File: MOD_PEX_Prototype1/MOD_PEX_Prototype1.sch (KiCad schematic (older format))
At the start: 69 parts, among them CN1 CONN_PANNEL_2X2, CN2 CONN_PANNEL_2X2, J1 RJ45_CHAIN, J2 RJ45_CHAIN, P1 HEADER_3X1, P2 HEADER_5X2, P3 HEADER_5X2, P4 HEADER_2X1, Q1 MMBT3904, Q2 MMBT3904, SW1 SWITCH_HH, U1 LPC111X_LQFP48, U2 AP1117E50G, U3 AP1117E33G, U4 SN75176BDR, X1 10MHz

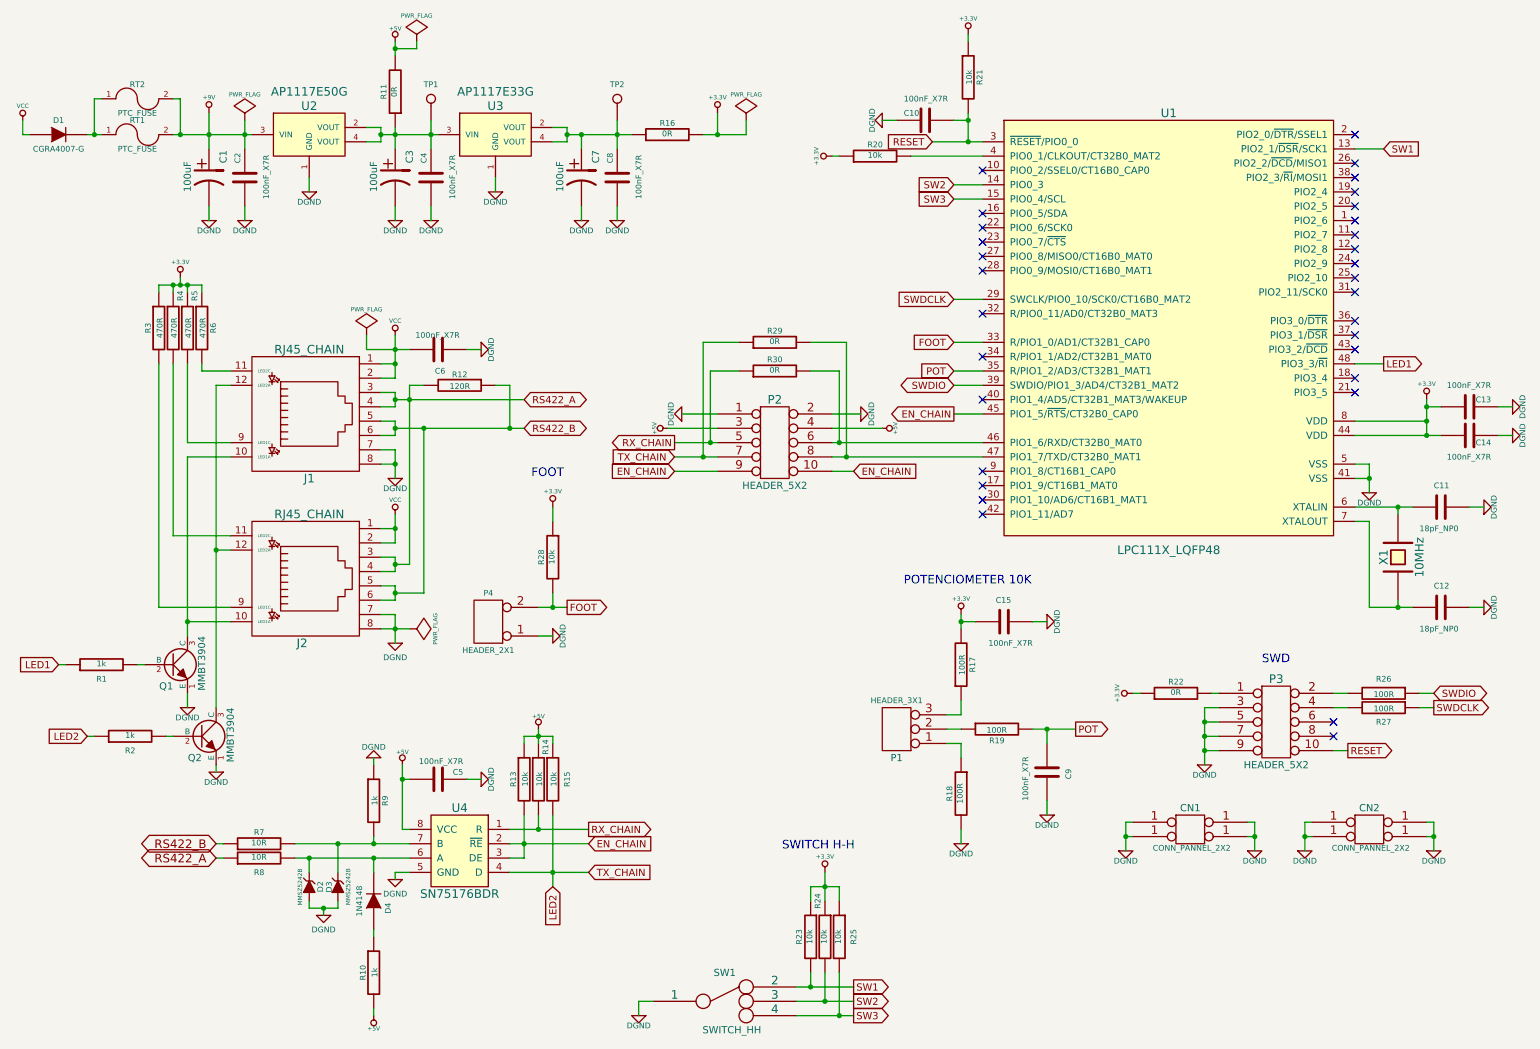
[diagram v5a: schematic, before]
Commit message: wip on issue #11: Use the same control chain circuit of the footswitch separated the schematics in subsheets and added the new control chain circuit and schematic symbols
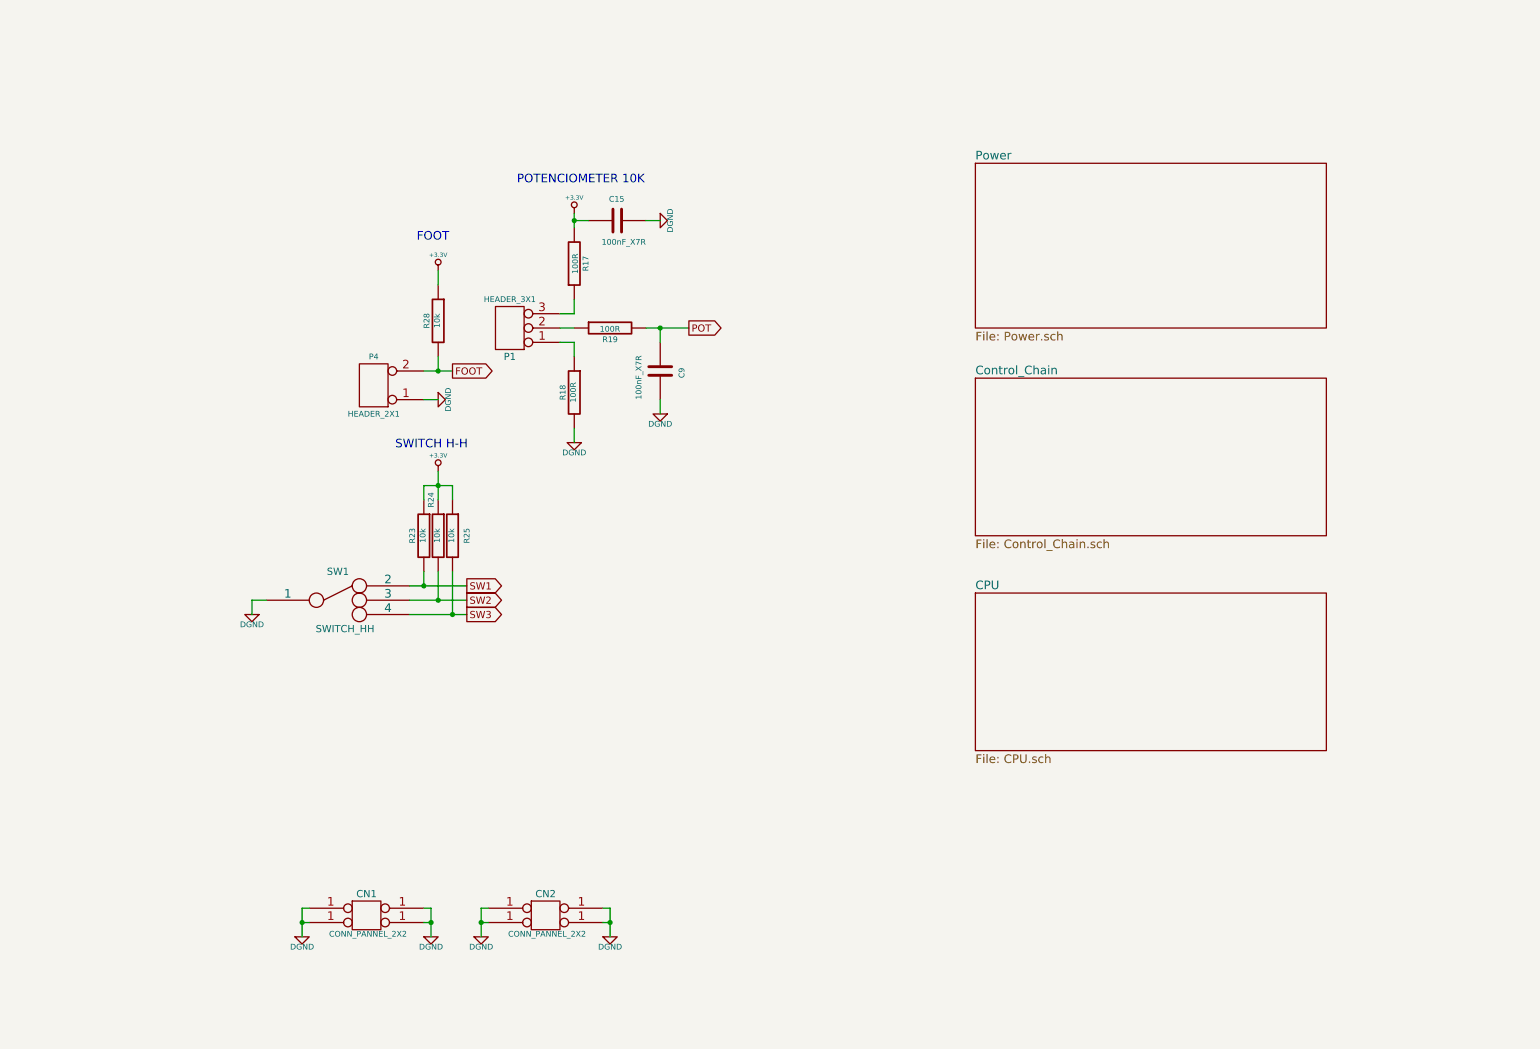
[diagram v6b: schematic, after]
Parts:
- removed C1, C3, C7: 100uF, MOD_Footprints_Lib:CAP_RAD_5MM, symbol CP1
- removed C10, C13, C14, C2, C4, C5, C6, C8: 100nF_X7R, MOD_Footprints_Lib:SM0603, symbol C
- removed C11, C12: 18pF_NP0, MOD_Footprints_Lib:SM0603, symbol C
- removed D1: CGRA4007-G, MOD_Footprints_Lib:DO-214AC(SMA), symbol DIODE
- removed D2, D3: MMSZ5242B, MOD_Footprints_Lib:SOD123, symbol ZENERsmall
- removed D4: 1N4148, MOD_Footprints_Lib:SOD323, symbol DIODE
- removed J1, J2: RJ45_CHAIN, MOD_Footprints_Lib:RJ45-RJHSE5084, symbol RJ45_CHAIN
- removed P2, P3: HEADER_5X2, MOD_Footprints_Lib:PIN_ARRAY_5x2, symbol CONN_5X2
- removed Q1, Q2: MMBT3904, MOD_Footprints_Lib:SOT23, symbol NPN
- removed R1, R10, R2, R9: 1k, MOD_Footprints_Lib:SM0603, symbol R
- removed R11, R16, R22, R29, R30: 0R, MOD_Footprints_Lib:SM0805, symbol R
- removed R12: 120R, MOD_Footprints_Lib:SM0805, symbol R
- removed R13, R14, R15, R20, R21: 10k, MOD_Footprints_Lib:SM0603, symbol R
- removed R26, R27: 100R, MOD_Footprints_Lib:SM0603, symbol R
- removed R3, R4, R5, R6: 470R, MOD_Footprints_Lib:SM0805, symbol R
- removed R7, R8: 10R, MOD_Footprints_Lib:SM0805, symbol R
- removed RT1: PTC_FUSE, MOD_Footprints_Lib:SM1210, symbol FUSE
- removed RT2: PTC_FUSE, MOD_Footprints_Lib:SM2920, symbol FUSE
- removed TP1, TP2: CONN_1, MOD_Footprints_Lib:SIL-1, symbol CONN_1
- removed U1: LPC111X_LQFP48, MOD_Footprints_Lib:LQFP48, symbol LPC111X_LQFP48
- removed U2: AP1117E50G, MOD_Footprints_Lib:SOT223_3, symbol LINEAR_REGULATOR_SOT223_3
- removed U3: AP1117E33G, MOD_Footprints_Lib:SOT223_3, symbol LINEAR_REGULATOR_SOT223_3
- removed U4: SN75176BDR, MOD_Footprints_Lib:SO8E, symbol SN75176BDR
- removed X1: 10MHz, MOD_Footprints_Lib:HC_49US, symbol CRYSTAL
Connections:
- no-connect marks 31 -> 0
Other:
- note removed: "SWD"
- moved on the sheet: C15, C9, CN1, CN2, P1, P4, R17, R18, R19, R23, R24, R25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
